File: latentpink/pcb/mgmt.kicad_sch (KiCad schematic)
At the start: 59 parts, among them J10 XILINX_JTAG, J11 FAN_01, J12 FAN_01, J15 CONN_01X03, J16 JUMPER_0402_SPDT, J17 JUMPER_0402_SPDT, J7 RJ45, U2 XC7K160T-2FBG484C, U20 AT24MAC402, U23 ADM3101E_QFN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

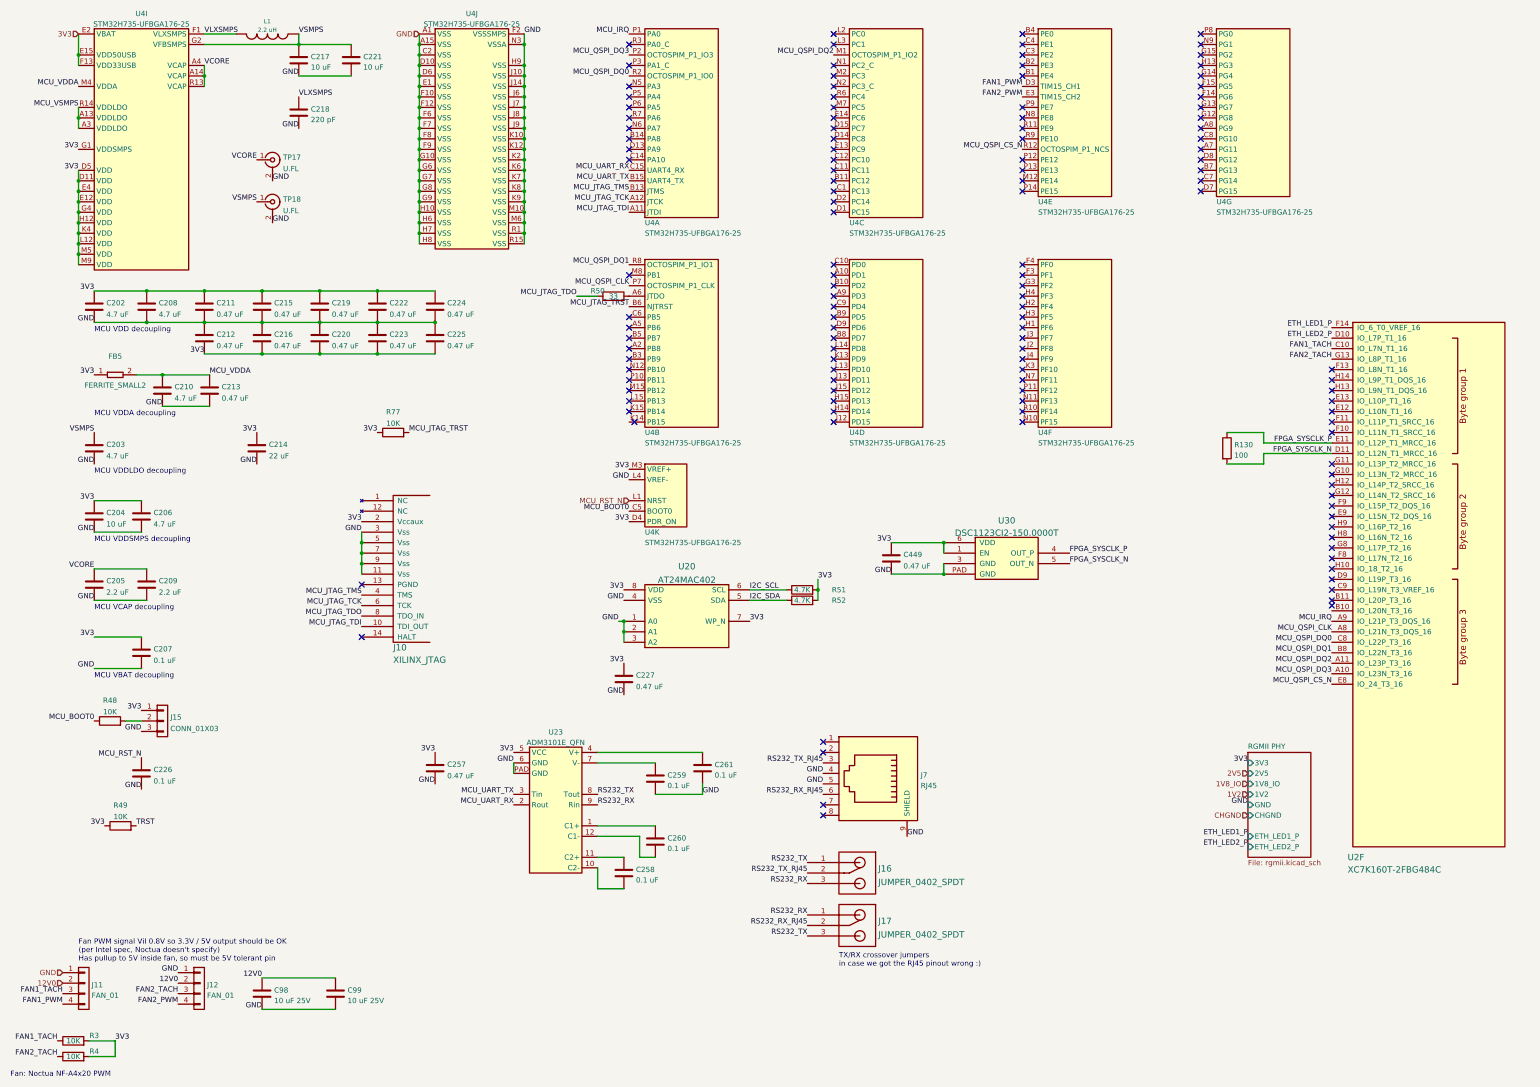
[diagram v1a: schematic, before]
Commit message: Finished initial schematic, ready for design review
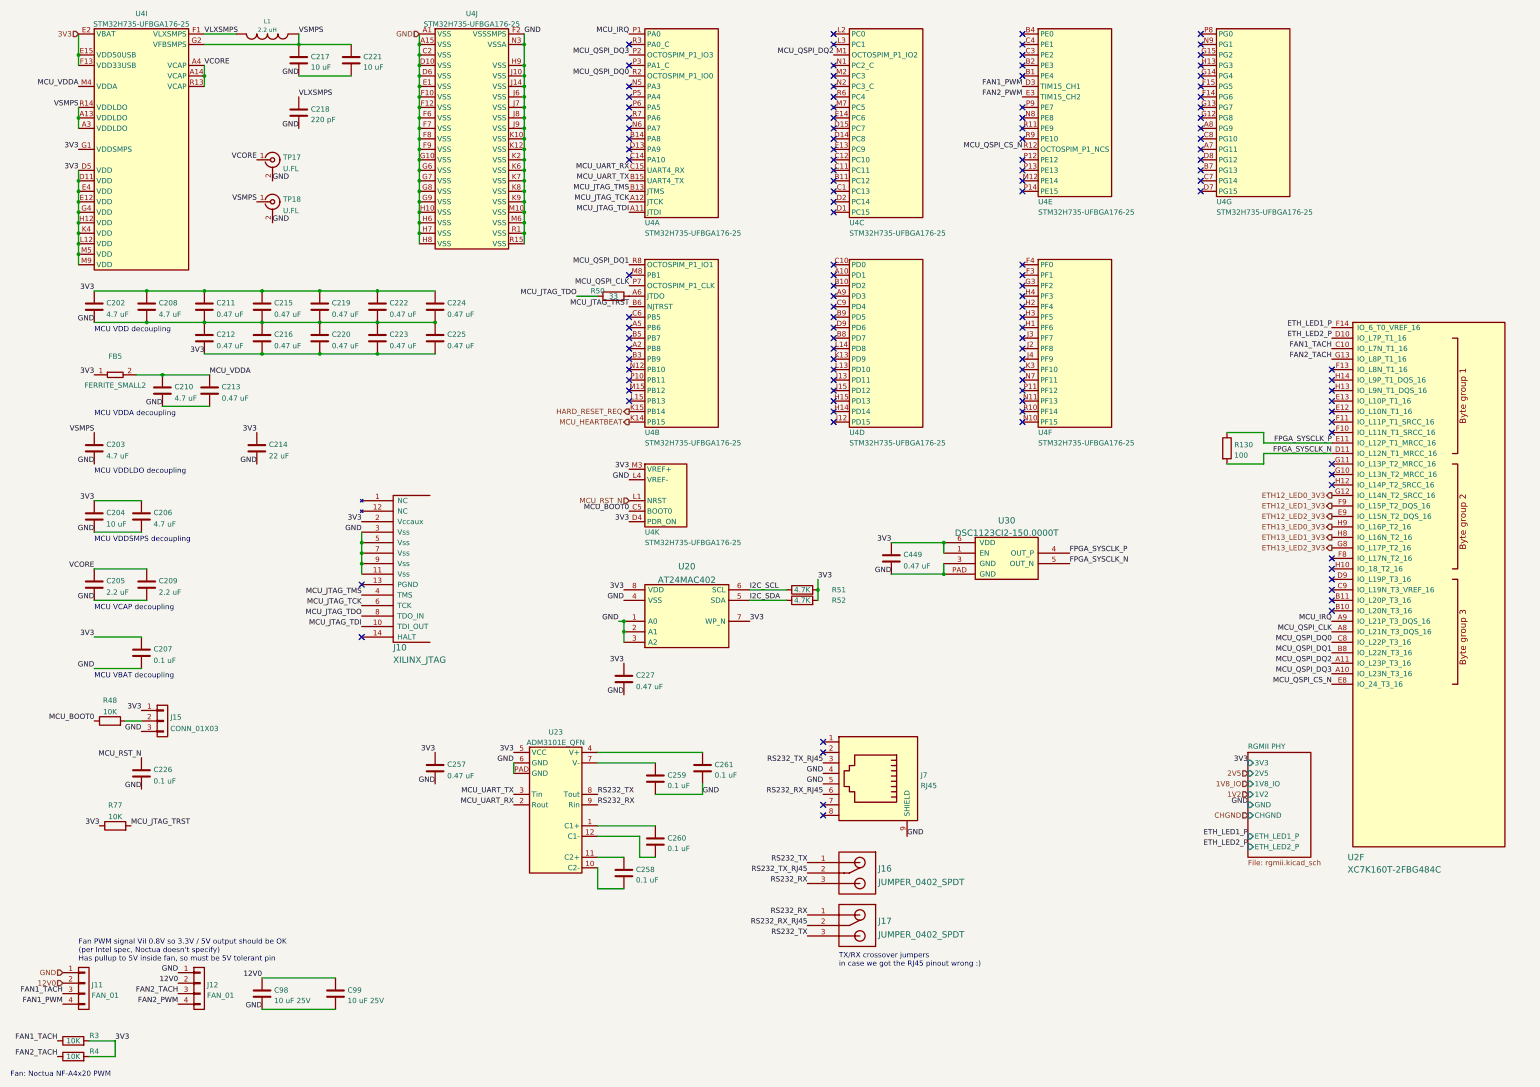
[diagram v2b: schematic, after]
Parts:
- removed R49: 10K, azonenberg_pcb:EIA_0402_RES_NOSILK, symbol device:R
- C217, C221: footprint (none) -> azonenberg_pcb:EIA_0805_CAP_NOSILK
- C218: footprint (none) -> azonenberg_pcb:EIA_0402_CAP_NOSILK
- L1: footprint (none) -> azonenberg_pcb:EIA_1210_CAP_NOSILK
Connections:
- net MCU_VSMPS is gone; now on net VSMPS: U4.A13 (VDDLDO), U4.A3 (VDDLDO), U4.R14 (VDDLDO)
- net ETH12_LED2_3V3: now reaches U2.E9 (IO_L15N_T2_DQS_16)
- net ETH12_LED1_3V3: now reaches U2.F9 (IO_L15P_T2_DQS_16)
- net ETH12_LED0_3V3: now reaches U2.G12 (IO_L14N_T2_SRCC_16)
- net ETH13_LED2_3V3: now reaches U2.G8 (IO_L17P_T2_16)
- net ETH13_LED1_3V3: now reaches U2.H8 (IO_L16N_T2_16)
- net ETH13_LED0_3V3: now reaches U2.H9 (IO_L16P_T2_16)
- net MCU_HEARTBEAT: now reaches U4.K14 (PB15)
- net HARD_RESET_REQ: now reaches U4.K15 (PB14)
- no-connect marks 128 -> 120
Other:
- moved on the sheet: R77
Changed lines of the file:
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@@
   (no_connect (at 260.35 93.98))
   (no_connect (at 260.35 60.96))
-  (no_connect (at 335.28 147.32))
   (no_connect (at 335.28 162.56))
-  (no_connect (at 335.28 149.86))
   (no_connect (at 335.28 137.16))
   (no_connect (at 335.28 132.08))
@@
   (no_connect (at 214.63 30.48))
   (no_connect (at 335.28 111.76))
-  (no_connect (at 335.28 139.7))
   (no_connect (at 214.63 111.76))
   (no_connect (at 260.35 121.92))
   (no_connect (at 214.63 38.1))
-  (no_connect (at 335.28 152.4))
-  (no_connect (at 165.1 119.38))
-  (no_connect (at 335.28 144.78))
   (no_connect (at 212.09 201.93))
   (no_connect (at 260.35 101.6))
@@
   (no_connect (at 165.1 96.52))
   (no_connect (at 303.53 58.42))
+  (no_connect (at 335.28 167.64))
   (no_connect (at 214.63 58.42))
   (no_connect (at 165.1 99.06))
@@
   (no_connect (at 214.63 63.5))
   (no_connect (at 165.1 114.3))
-  (no_connect (at 335.28 142.24))
   (no_connect (at 260.35 86.36))
   (no_connect (at 165.1 55.88))
@@
   (no_connect (at 260.35 50.8))
   (no_connect (at 214.63 101.6))
-  (no_connect (at 166.37 121.92))
   (no_connect (at 335.28 124.46))
   (no_connect (at 260.35 33.02))
@@
   (no_connect (at 260.35 66.04))
   (no_connect (at 335.28 114.3))
-  (no_connect (at 335.28 166.37))
   (no_connect (at 260.35 53.34))
   (no_connect (at 214.63 66.04))
@@
     (effects (font (size 1.27 1.27)) (justify right bottom))
   )
-  (label "TRST" (at 45.72 219.71 0)
-    (effects (font (size 1.27 1.27)) (justify left bottom))
-  )
   (label "12V0" (at 55.88 257.81 180)
     (effects (font (size 1.27 1.27)) (justify right bottom))
   )
-  (label "MCU_VSMPS" (at 31.75 45.72 180)
+  (label "VSMPS" (at 31.75 45.72 180)
     (effects (font (size 1.27 1.27)) (justify right bottom))
   )
@@
     (effects (font (size 1.27 1.27)) (justify right bottom))
   )
-  (label "3V3" (at 38.1 219.71 180)
-    (effects (font (size 1.27 1.27)) (justify right bottom))
-  )
   (label "3V3" (at 314.96 204.47 180)
     (effects (font (size 1.27 1.27)) (justify right bottom))
@@
     (effects (font (size 1.27 1.27)) (justify right bottom))
   )
-  (label "3V3" (at 104.14 124.46 180)
+  (label "3V3" (at 36.83 219.71 180)
     (effects (font (size 1.27 1.27)) (justify right bottom))
   )
@@
     (effects (font (size 1.27 1.27)) (justify right bottom))
   )
-  (label "MCU_JTAG_TRST" (at 111.76 124.46 0)
+  (label "MCU_JTAG_TRST" (at 44.45 219.71 0)
     (effects (font (size 1.27 1.27)) (justify left bottom))
   )
@@
     (effects (font (size 1.27 1.27)) (justify right))
   )
+  (hierarchical_label "HARD_RESET_REQ" (shape output) (at 165.1 119.38 180)
+    (effects (font (size 1.27 1.27)) (justify right))
+  )
   (hierarchical_label "1V2" (shape input) (at 314.96 212.09 180)
     (effects (font (size 1.27 1.27)) (justify right))
   )
+  (hierarchical_label "ETH13_LED2_3V3" (shape output) (at 335.28 152.4 180)
+    (effects (font (size 1.27 1.27)) (justify right))
+  )
+  (hierarchical_label "ETH12_LED1_3V3" (shape output) (at 335.28 142.24 180)
+    (effects (font (size 1.27 1.27)) (justify right))
+  )
+  (hierarchical_label "MCU_HEARTBEAT" (shape output) (at 165.1 121.92 180)
+    (effects (font (size 1.27 1.27)) (justify right))
+  )
   (hierarchical_label "2V5" (shape input) (at 314.96 207.01 180)
     (effects (font (size 1.27 1.27)) (justify right))
   )
+  (hierarchical_label "ETH13_LED0_3V3" (shape output) (at 335.28 147.32 180)
+    (effects (font (size 1.27 1.27)) (justify right))
+  )
+  (hierarchical_label "ETH12_LED0_3V3" (shape output) (at 335.28 139.7 180)
+    (effects (font (size 1.27 1.27)) (justify right))
+  )
   (hierarchical_label "GND" (shape input) (at 27.94 255.27 180)
     (effects (font (size 1.27 1.27)) (justify right))
   )
+  (hierarchical_label "ETH13_LED1_3V3" (shape output) (at 335.28 149.86 180)
+    (effects (font (size 1.27 1.27)) (justify right))
+  )
+  (hierarchical_label "ETH12_LED2_3V3" (shape output) (at 335.28 144.78 180)
+    (effects (font (size 1.27 1.27)) (justify right))
+  )
   (hierarchical_label "3V3" (shape input) (at 31.75 27.94 180)
     (effects (font (size 1.27 1.27)) (justify right))
@@
       (effects (font (size 1.27 1.27)) (justify left))
     )
-    (property "Footprint" "" (id 2) (at 86.0552 38.1 0)
+    (property "Footprint" "azonenberg_pcb:EIA_0805_CAP_NOSILK" (id 2) (at 86.0552 38.1 0)
       (effects (font (size 1.27 1.27)) hide)
     )
@@
     (pin "2")
   )
-  (symbol (lib_id "device:R") (at 107.95 124.46 90) (unit 1)
+  (symbol (lib_id "device:R") (at 40.64 219.71 90) (unit 1)
     (in_bom yes) (on_board yes) (fields_autoplaced)
-    (property "Reference" "R77" (id 0) (at 107.95 119.4775 90))
-    (property "Value" "10K" (id 1) (at 107.95 122.2526 90))
-    (property "Footprint" "azonenberg_pcb:EIA_0402_RES_NOSILK" (id 2) (at 107.95 126.238 90)
+    (property "Reference" "R77" (id 0) (at 40.64 214.7275 90))
+    (property "Value" "10K" (id 1) (at 40.64 217.5026 90))
+    (property "Footprint" "azonenberg_pcb:EIA_0402_RES_NOSILK" (id 2) (at 40.64 221.488 90)
       (effects (font (size 1.27 1.27)) hide)
     )
-    (property "Datasheet" "" (id 3) (at 107.95 124.46 0)
+    (property "Datasheet" "" (id 3) (at 40.64 219.71 0)
       (effects (font (size 1.27 1.27)) hide)
     )
@@
       (effects (font (size 1.27 1.27)) (justify left))
     )
-    (property "Footprint" "" (id 2) (at 98.7552 38.1 0)
+    (property "Footprint" "azonenberg_pcb:EIA_0805_CAP_NOSILK" (id 2) (at 98.7552 38.1 0)
       (effects (font (size 1.27 1.27)) hide)
     )
@@
       (effects (font (size 1.27 1.27)) (justify left))
     )
-    (property "Footprint" "" (id 2) (at 86.0552 50.8 0)
+    (property "Footprint" "azonenberg_pcb:EIA_0402_CAP_NOSILK" (id 2) (at 86.0552 50.8 0)
       (effects (font (size 1.27 1.27)) hide)
     )
@@
       (effects (font (size 1.016 1.016)))
     )
-    (property "Footprint" "" (id 2) (at 77.47 27.94 0)
+    (property "Footprint" "azonenberg_pcb:EIA_1210_CAP_NOSILK" (id 2) (at 77.47 27.94 0)
       (effects (font (size 1.524 1.524)) hide)
     )
@@
       (effects (font (size 1.27 1.27)) hide)
     )
-    (pin "1")
-    (pin "2")
-  )
-  (symbol (lib_id "device:R") (at 41.91 219.71 90) (unit 1)
-    (in_bom yes) (on_board yes) (fields_autoplaced)
-    (property "Reference" "R49" (id 0) (at 41.91 214.7275 90))
-    (property "Value" "10K" (id 1) (at 41.91 217.5026 90))
-    (property "Footprint" "azonenberg_pcb:EIA_0402_RES_NOSILK" (id 2) (at 41.91 221.488 90)
-      (effects (font (size 1.27 1.27)) hide)
-    )
-    (property "Datasheet" "" (id 3) (at 41.91 219.71 0)
-      (effects (font (size 1.27 1.27)) hide)
-    )

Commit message: Added some debug LEDs, PMOD, and temp sensors
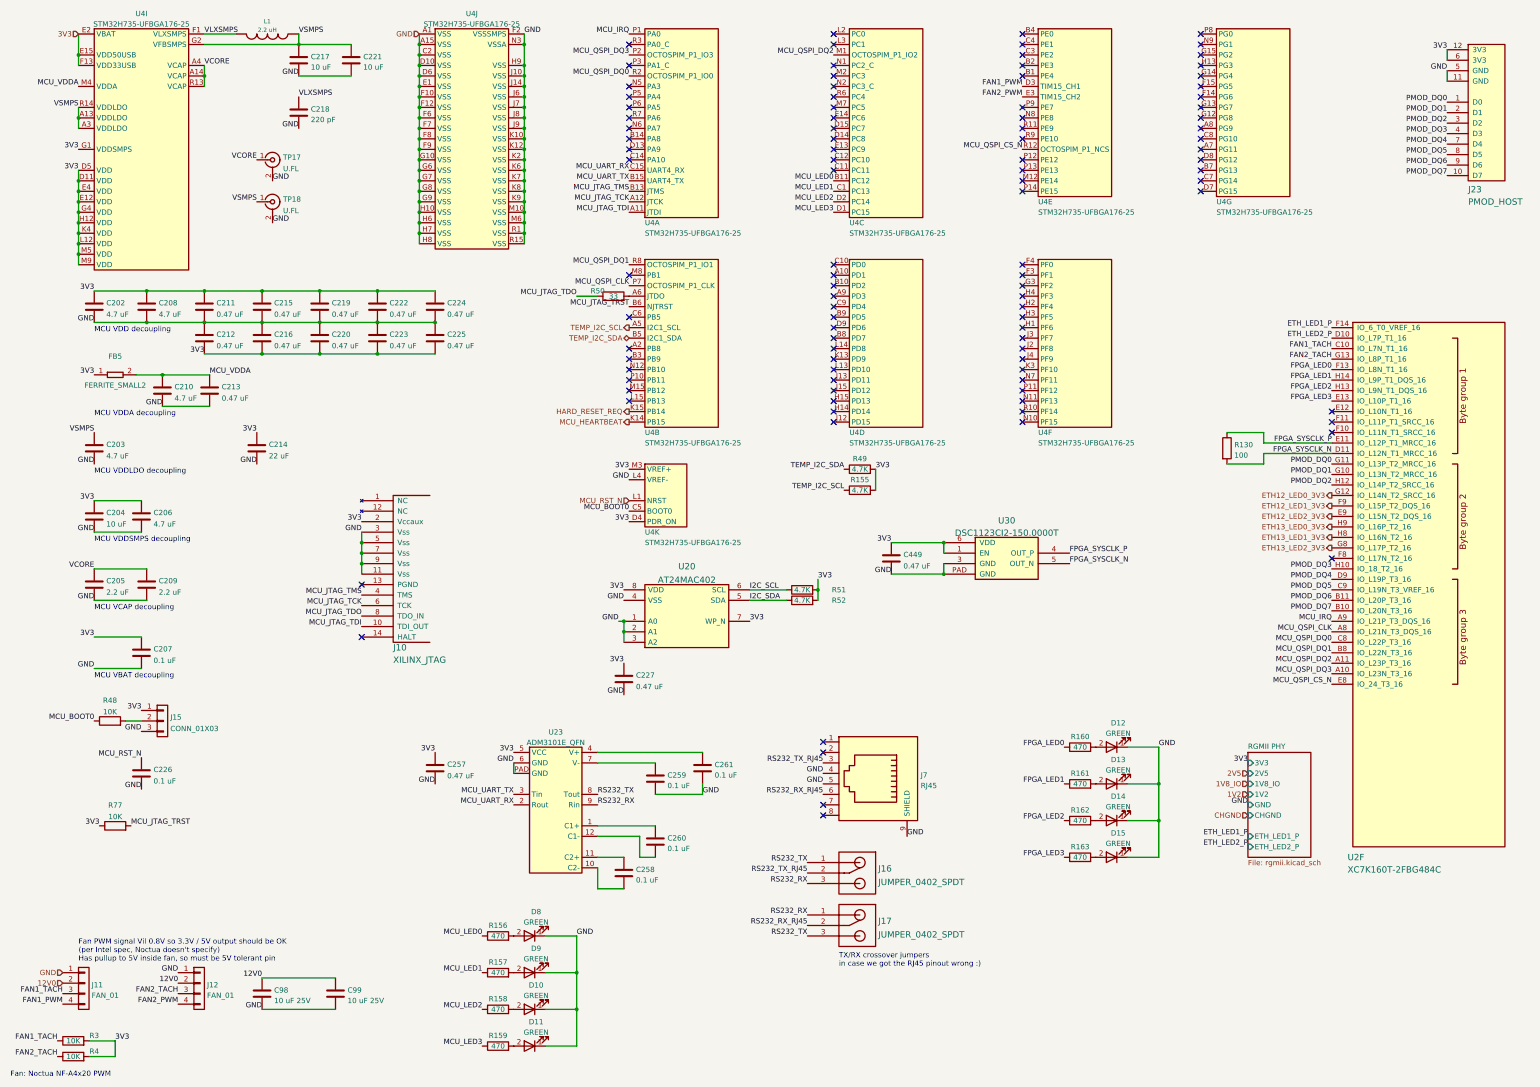
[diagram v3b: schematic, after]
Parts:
- added D10, D11, D12, D13, D14, D15, D8, D9: GREEN, azonenberg_pcb:EIA_0603_LED, symbol device:LED
- added J23: PMOD_HOST, azonenberg_pcb:CONN_HEADER_2.54MM_2x6_RA_PMOD_HOST, symbol special-azonenberg:PMOD_HOST
- added R155, R49: 4.7K, azonenberg_pcb:EIA_0402_RES_NOSILK, symbol device:R
- added R156, R157, R158, R159, R160, R161, R162, R163: 470, azonenberg_pcb:EIA_0402_RES_NOSILK, symbol device:R
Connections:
- net 3V3: now also J23.12 (3V3), J23.6 (3V3), R155.2, R49.2
- net GND: now also D10.1 (K), D11.1 (K), D12.1 (K), D13.1 (K), D14.1 (K), D15.1 (K), D8.1 (K), D9.1 (K), J23.11 (GND), J23.5 (GND)
- net PMOD_DQ7: now reaches U2.B10 (IO_L20N_T3_16)
- net PMOD_DQ7: now also J23.10 (D7)
- net PMOD_DQ6: now reaches U2.B11 (IO_L20P_T3_16)
- net PMOD_DQ6: now also J23.9 (D6)
- net PMOD_DQ5: now reaches U2.C9 (IO_L19N_T3_VREF_16)
- net PMOD_DQ5: now also J23.8 (D5)
- net PMOD_DQ4: now reaches U2.D9 (IO_L19P_T3_16)
- net PMOD_DQ4: now also J23.7 (D4)
- net FPGA_LED3: now reaches U2.E13 (IO_L10P_T1_16)
- net FPGA_LED3: now also R163.1
- net FPGA_LED0: now reaches U2.F13 (IO_L8N_T1_16)
- net FPGA_LED0: now also R160.1
- net PMOD_DQ1: now reaches U2.G10 (IO_L13N_T2_MRCC_16)
- net PMOD_DQ1: now also J23.2 (D1)
- net PMOD_DQ0: now reaches U2.G11 (IO_L13P_T2_MRCC_16)
- net PMOD_DQ0: now also J23.1 (D0)
- net PMOD_DQ3: now reaches U2.H10 (IO_18_T2_16)
- net PMOD_DQ3: now also J23.4 (D3)
- net PMOD_DQ2: now reaches U2.H12 (IO_L14P_T2_SRCC_16)
- net PMOD_DQ2: now also J23.3 (D2)
- net FPGA_LED2: now reaches U2.H13 (IO_L9N_T1_DQS_16)
- net FPGA_LED2: now also R162.1
- net FPGA_LED1: now reaches U2.H14 (IO_L9P_T1_DQS_16)
- net FPGA_LED1: now also R161.1
- net MCU_LED0: now reaches U4.B11 (PC12)
- net MCU_LED0: now also R156.1
- net MCU_LED1: now reaches U4.C1 (PC13)
- net MCU_LED1: now also R157.1
- net MCU_LED3: now reaches U4.D1 (PC15)
- net MCU_LED3: now also R159.1
- net MCU_LED2: now reaches U4.D2 (PC14)
- net MCU_LED2: now also R158.1
- net TEMP_I2C_SCL: now reaches U4.A5 (PB6)
- net TEMP_I2C_SCL: now also R155.1
- net TEMP_I2C_SDA: now reaches U4.B5 (PB7)
- net TEMP_I2C_SDA: now also R49.1
- new net: D10.2 (A), R158.2
- new net: D9.2 (A), R157.2
- new net: D8.2 (A), R156.2
- new net: D12.2 (A), R160.2
- new net: D15.2 (A), R163.2
- new net: D14.2 (A), R162.2
- new net: D13.2 (A), R161.2
- new net: D11.2 (A), R159.2
- no-connect marks 120 -> 102
